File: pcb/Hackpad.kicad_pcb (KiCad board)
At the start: 2 copper layers, 109.6 x 70.4 mm, 21 parts, among them SW1 SW_Push, SW10 RotaryEncoder, SW2 SW_Push, SW3 SW_Push, SW4 SW_Push, SW5 SW_Push, SW6 SW_Push, SW7 SW_Push, SW8 SW_Push, SW9 SW_Push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

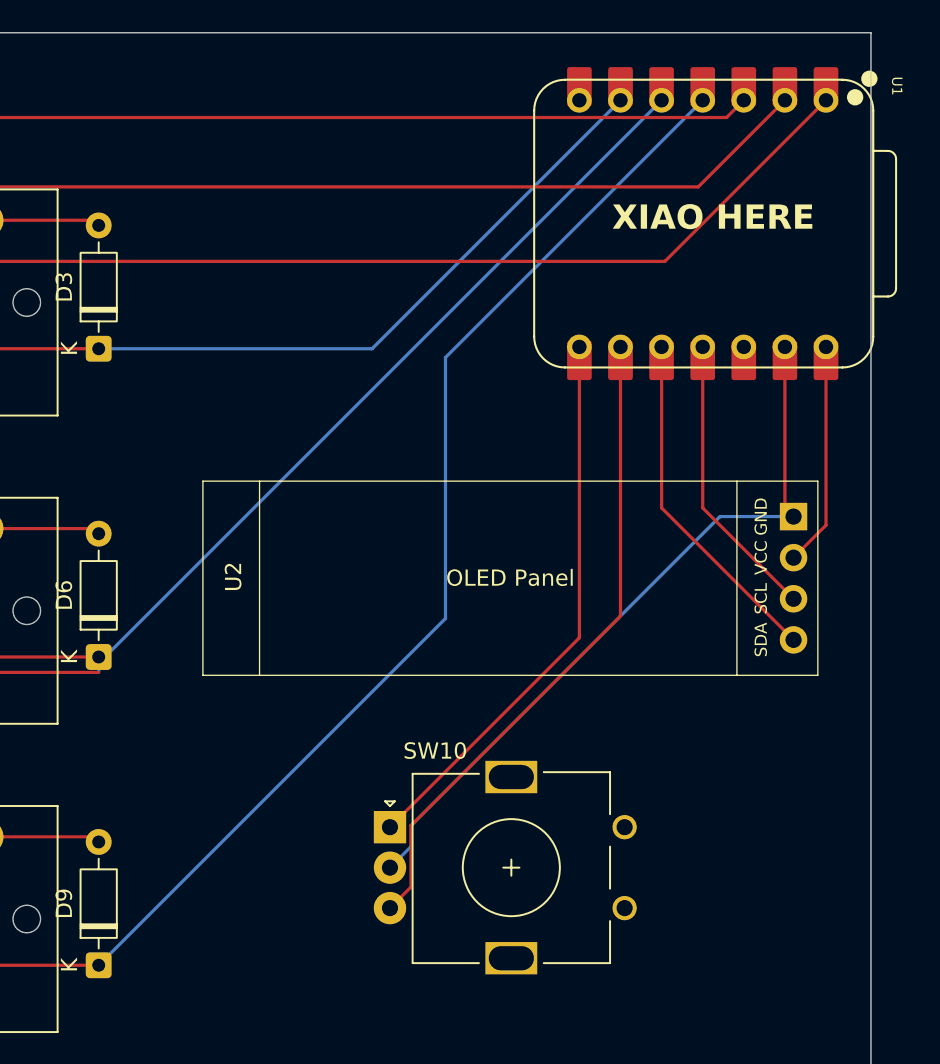
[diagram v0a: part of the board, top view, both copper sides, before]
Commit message: fix OLED schematic and pcb OLED wiring
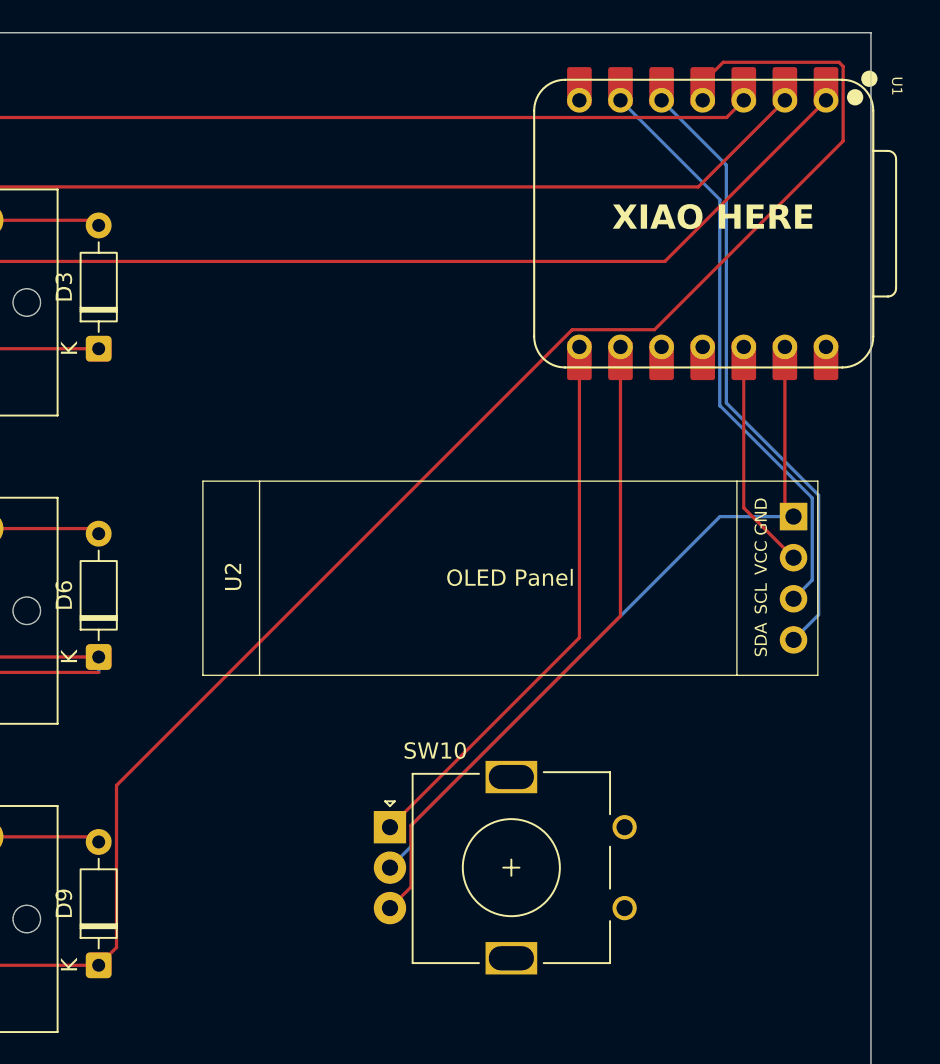
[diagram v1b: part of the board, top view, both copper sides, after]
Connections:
- U1 pad 10: OL_SDA -> Row 4
- U1 pad 11: OL_SCL -> Row 3
- U1 pad 12: unconnected-(U1-3V3-Pad12) -> Net-(U1-3V3)
- U1 pad 5: Row 1 -> OL_SDA
- U1 pad 6: Row 0 -> OL_SCL
- U2 pad 2: +5V -> Net-(U1-3V3)
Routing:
- net Row 1: track 106.9 -> 57.7 mm
- net Row 0: track 76.7 -> 38.1 mm
- net OL_SCL: track 17.1 -> 36.2 mm
- net Row 2: track 107.0 -> 126.1 mm
- net OL_SDA: track 21.5 -> 38.0 mm
- net Net-(U1-3V3): track 0.00 -> 14.3 mm
- net +5V: track 13.0 -> 0.00 mm

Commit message: fix matrix wiring issue
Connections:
- U1 pad 10: Row 4 -> Row 0
- U1 pad 11: Row 3 -> Row 1
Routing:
- net Row 0: track 38.1 -> 73.8 mm
- net Row 1: track 57.7 -> 83.9 mm
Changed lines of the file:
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@@
 	(net 21 "OL_SDA")
 	(net 22 "OL_SCL")
-	(net 23 "Row 4")
-	(net 24 "Row 3")
-	(net 25 "Net-(U1-3V3)")
+	(net 23 "Net-(U1-3V3)")
 	(footprint "Button_Switch_Keyboard:SW_Cherry_MX_1.00u_PCB"
 		(layer "F.Cu")
@@
 			(layers "*.Cu" "*.Mask")
 			(remove_unused_layers no)
-			(net 23 "Row 4")
+			(net 4 "Row 0")
 			(pinfunction "GPIO4/MISO")
 			(pintype "passive")
@@
 			(layers "F.Cu" "F.Mask")
 			(roundrect_rratio 0.1)
-			(net 23 "Row 4")
+			(net 4 "Row 0")
 			(pinfunction "GPIO4/MISO")
 			(pintype "passive")
@@
 			(layers "*.Cu" "*.Mask")
 			(remove_unused_layers no)
-			(net 24 "Row 3")
+			(net 9 "Row 1")
 			(pinfunction "GPIO3/MOSI")
 			(pintype "passive")
@@
 			(layers "F.Cu" "F.Mask")
 			(roundrect_rratio 0.1)
-			(net 24 "Row 3")
+			(net 9 "Row 1")
 			(pinfunction "GPIO3/MOSI")
 			(pintype "passive")
@@
 			(layers "*.Cu" "*.Mask")
 			(remove_unused_layers no)
-			(net 25 "Net-(U1-3V3)")
+			(net 23 "Net-(U1-3V3)")
 			(pinfunction "3V3")
 			(pintype "passive")
@@
 			(layers "F.Cu" "F.Mask")
 			(roundrect_rratio 0.1)
-			(net 25 "Net-(U1-3V3)")
+			(net 23 "Net-(U1-3V3)")
 			(pinfunction "3V3")
 			(pintype "passive")
@@
 			(layers "*.Cu" "*.Mask")
 			(remove_unused_layers no)
-			(net 25 "Net-(U1-3V3)")
+			(net 23 "Net-(U1-3V3)")
 			(pinfunction "VCC")
 			(pintype "power_in")
@@
 	)
 	(segment
+		(start 214.697 68.357)
+		(end 182.1505 68.357)
+		(width 0.2)
+		(layer "B.Cu")
+		(net 4)
+	)
+	(segment
+		(start 215.76 69.42)
+		(end 214.697 68.357)
+		(width 0.2)
+		(layer "B.Cu")
+		(net 4)
+	)
+	(segment
+		(start 182.1505 68.357)
+		(end 180.975 69.5325)
+		(width 0.2)
+		(layer "B.Cu")
+		(net 4)
+	)
+	(segment
 		(start 142.5575 61.595)
 		(end 142.875 61.9125)
@@
 	)
 	(segment
-		(start 180.975 89.535)
-		(end 142.875 89.535)
+		(start 142.875 88.5825)
+		(end 161.925 88.5825)
 		(width 0.2)
 		(layer "F.Cu")
@@
 	)
 	(segment
+		(start 218.3 69.42)
+		(end 199.1375 88.5825)
+		(width 0.2)
+		(layer "B.Cu")
+		(net 9)
+	)
+	(segment
 		(start 180.975 88.965)
 		(end 180.975 89.535)
@@
 	)
 	(segment
+		(start 199.1375 88.5825)
+		(end 180.975 88.5825)
+		(width 0.2)
+		(layer "B.Cu")
+		(net 9)
+	)
+	(segment
 		(start 161.6075 80.645)
 		(end 161.925 80.9625)
@@
 		(width 0.2)
 		(layer "F.Cu")
-		(net 25)
+		(net 23)
 	)
 	(segment
@@
 		(width 0.2)
 		(layer "F.Cu")
-		(net 25)
+		(net 23)
 	)
 	(embedded_fonts no)
